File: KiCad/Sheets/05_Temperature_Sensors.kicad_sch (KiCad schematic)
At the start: 7 parts, among them U4 GAS_FLOW_SENSOR, U5 GAS_RETURN_SENSOR, U6 WOOD_FLOW_SENSOR, U7 WOOD_RETURN_SENSOR, U8 WOOD_BOILER_SENSOR

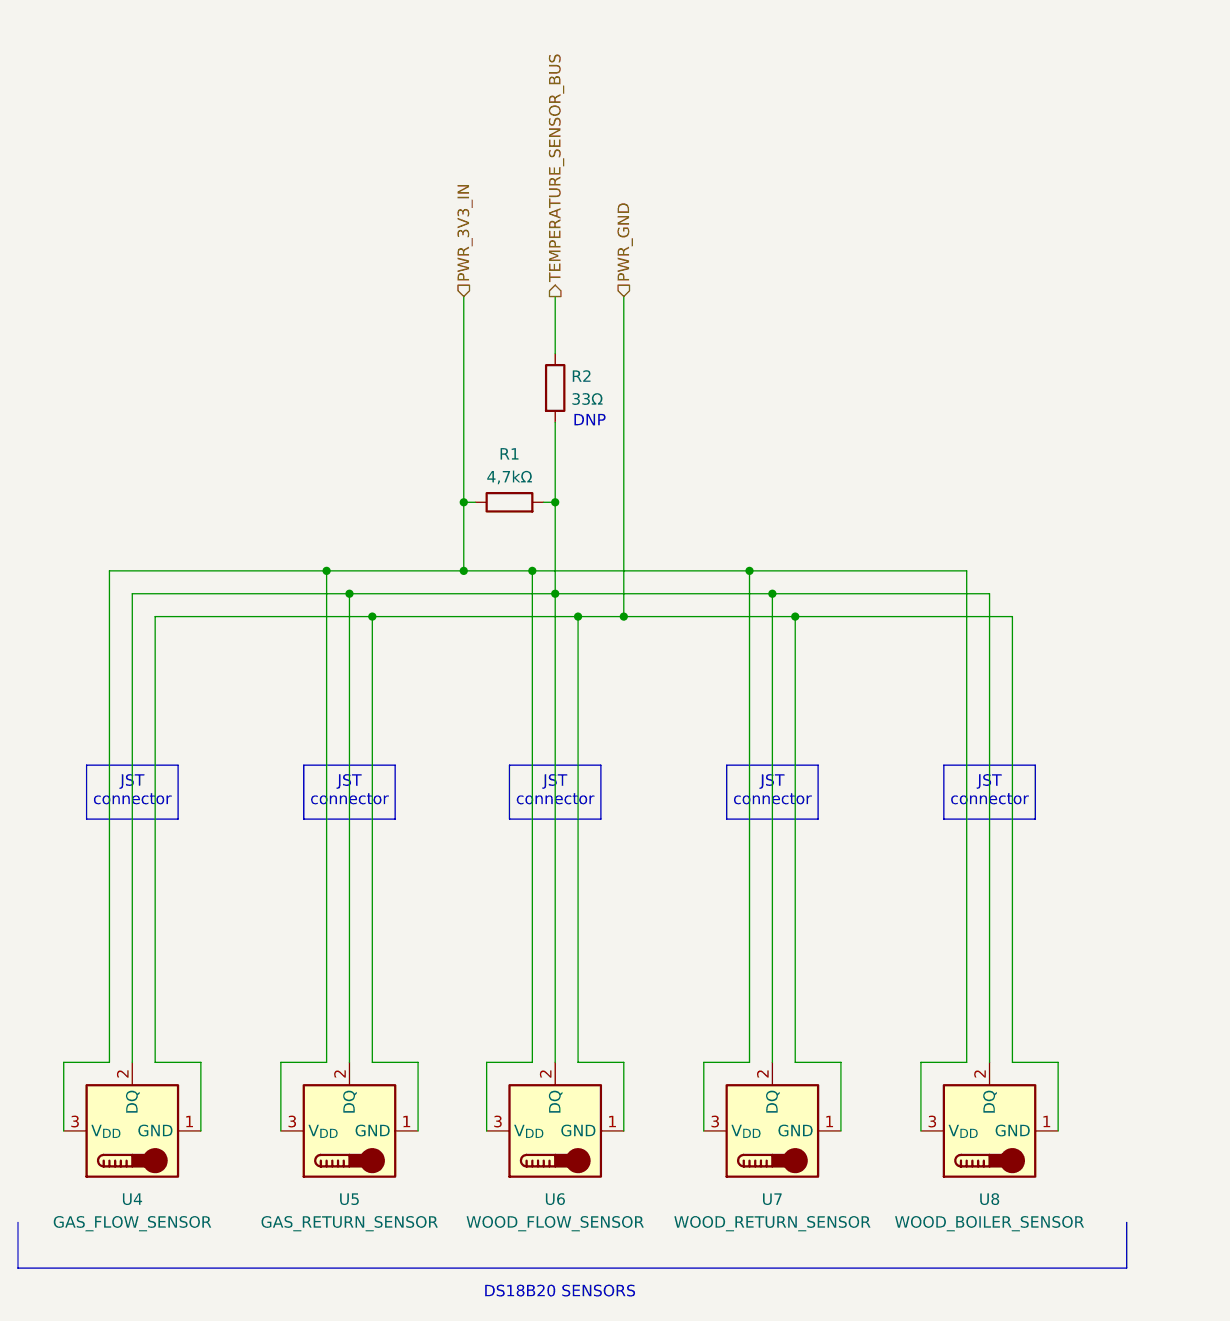
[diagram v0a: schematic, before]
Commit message: Footprints are created and assigned
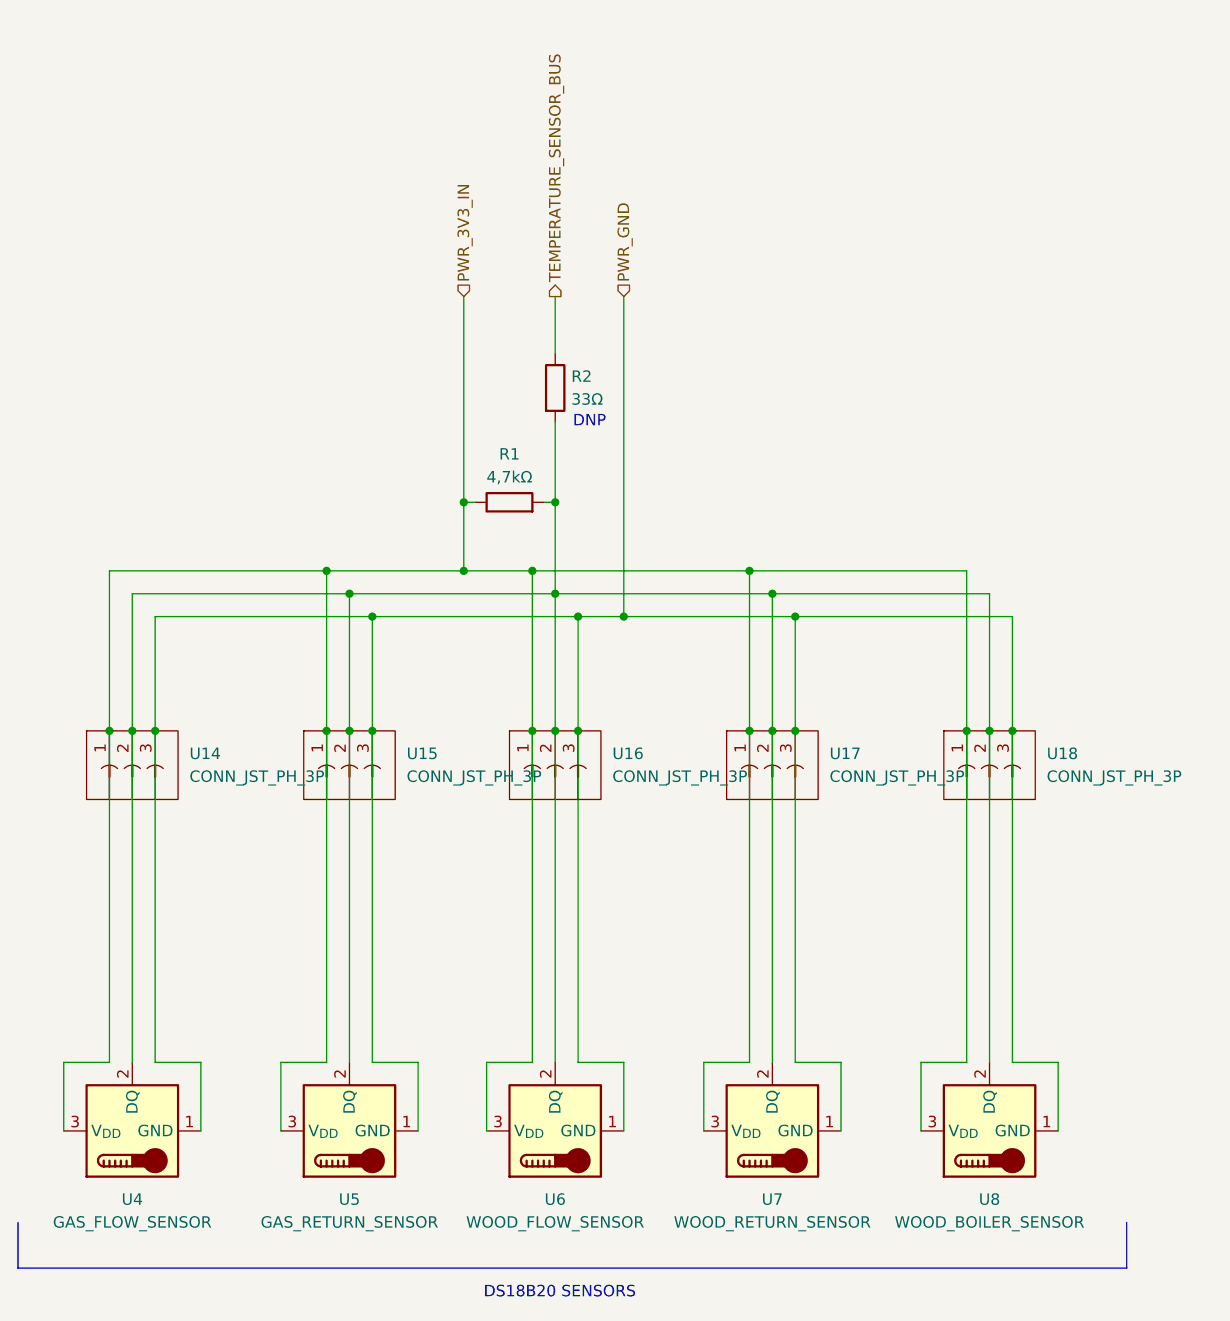
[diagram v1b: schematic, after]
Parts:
- added U14, U15, U16, U17, U18: CONN_JST_PH_3P, Connector_JST:JST_PH_B3B-PH-K_1x03_P2.00mm_Vertical, symbol HMS_Symbols:CONN_JST_PH_3P
- R1, R2: footprint (none) -> Resistor_THT:R_Axial_DIN0207_L6.3mm_D2.5mm_P7.62mm_Horizontal
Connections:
- net PWR_3V3_IN: now also U14.1, U15.1, U16.1, U17.1, U18.1
- net PWR_GND: now also U14.3, U15.3, U16.3, U17.3, U18.3
- net at R1.2, R2.2, U4.2 (DQ)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: now also U14.2, U15.2, U16.2, U17.2, U18.2

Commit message: LEDs sheet added, schematic finished
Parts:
- U14: value CONN_JST_PH_3P -> GAS_FLOW_SENSOR_SOCKET
- U15: value CONN_JST_PH_3P -> GAS_RETURN_SENSOR_SOCKET
- U16: value CONN_JST_PH_3P -> WOOD_FLOW_SENSOR_SOCKET
- U17: value CONN_JST_PH_3P -> WOOD_RETURN_SENSOR_SOCKET
- U18: value CONN_JST_PH_3P -> WOOD_BOILER_SENSOR_SOCKET
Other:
- note removed: "DNP"
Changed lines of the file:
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@@
 	(generator_version "10.0")
 	(paper "A4")
-	(text "DNP"
-		(exclude_from_sim no)
-		(at 151.13 62.23 0)
-		(effects
-			(font
-				(size 1.27 1.27)
-			)
-		)
-	)
 	(text "DS18B20 SENSORS"
 		(exclude_from_sim no)
@@
 		(at 124.46 96.52)
 		(diameter 0)
-		(color 0 0 0 0)
+		(color 255 153 0 1)
 	)
 	(junction
 		(at 171.45 96.52)
 		(diameter 0)
-		(color 0 0 0 0)
+		(color 255 153 0 1)
 	)
 	(junction
@@
 		(at 173.99 96.52)
 		(diameter 0)
-		(color 0 0 0 0)
+		(color 0 0 0 1)
 	)
 	(junction
@@
 		(at 144.78 96.52)
 		(diameter 0)
-		(color 0 0 0 0)
+		(color 255 0 0 1)
 	)
 	(junction
 		(at 147.32 96.52)
 		(diameter 0)
-		(color 0 0 0 0)
+		(color 255 153 0 1)
 	)
 	(junction
 		(at 198.12 96.52)
 		(diameter 0)
-		(color 0 0 0 0)
+		(color 0 0 0 1)
 	)
 	(junction
@@
 		(at 193.04 96.52)
 		(diameter 0)
-		(color 0 0 0 0)
+		(color 255 0 0 1)
 	)
 	(junction
@@
 		(at 168.91 96.52)
 		(diameter 0)
-		(color 0 0 0 0)
+		(color 255 0 0 1)
 	)
 	(junction
 		(at 149.86 96.52)
 		(diameter 0)
-		(color 0 0 0 0)
+		(color 0 0 0 1)
 	)
 	(junction
 		(at 195.58 96.52)
 		(diameter 0)
-		(color 0 0 0 0)
+		(color 255 153 0 1)
 	)
 	(junction
 		(at 97.79 96.52)
 		(diameter 0)
-		(color 0 0 0 0)
+		(color 255 0 0 1)
 	)
 	(junction
 		(at 100.33 96.52)
 		(diameter 0)
-		(color 0 0 0 0)
+		(color 255 153 0 1)
 	)
 	(junction
@@
 		(at 127 96.52)
 		(diameter 0)
-		(color 0 0 0 0)
+		(color 0 0 0 1)
 	)
 	(junction
@@
 		(at 121.92 96.52)
 		(diameter 0)
-		(color 0 0 0 0)
+		(color 255 0 0 1)
 	)
 	(junction
 		(at 102.87 96.52)
 		(diameter 0)
-		(color 0 0 0 0)
+		(color 0 0 0 1)
 	)
 	(junction
@@
 		(in_pos_files yes)
 		(dnp no)
-		(fields_autoplaced yes)
 		(property "Reference" "U15"
 			(at 130.81 99.0599 0)
@@
 			)
 		)
-		(property "Value" "CONN_JST_PH_3P"
-			(at 130.81 101.5999 0)
+		(property "Value" "GAS_RETURN_SENSOR_SOCKET"
+			(at 110.744 93.726 0)
 			(show_name no)
 			(do_not_autoplace no)
@@
 		(in_pos_files yes)
 		(dnp no)
-		(fields_autoplaced yes)
 		(property "Reference" "U14"
 			(at 106.68 99.0599 0)
@@
 			)
 		)
-		(property "Value" "CONN_JST_PH_3P"
-			(at 106.68 101.5999 0)
+		(property "Value" "GAS_FLOW_SENSOR_SOCKET"
+			(at 89.154 105.918 0)
 			(show_name no)
 			(do_not_autoplace no)
@@
 		(in_pos_files yes)
 		(dnp no)
-		(fields_autoplaced yes)
 		(property "Reference" "U16"
 			(at 153.67 99.0599 0)
@@
 			)
 		)
-		(property "Value" "CONN_JST_PH_3P"
-			(at 153.67 101.5999 0)
+		(property "Value" "WOOD_FLOW_SENSOR_SOCKET"
+			(at 134.112 106.172 0)
 			(show_name no)
 			(do_not_autoplace no)
@@
 		(in_pos_files yes)
 		(dnp no)
-		(fields_autoplaced yes)
 		(property "Reference" "U18"
 			(at 201.93 99.0599 0)
@@
 			)
 		)
-		(property "Value" "CONN_JST_PH_3P"
-			(at 201.93 101.5999 0)
+		(property "Value" "WOOD_BOILER_SENSOR_SOCKET"
+			(at 180.848 105.918 0)
 			(show_name no)
 			(do_not_autoplace no)
@@
 		(in_pos_files yes)
 		(dnp no)
-		(fields_autoplaced yes)
 		(property "Reference" "U17"
 			(at 177.8 99.0599 0)
@@
 			)
 		)
-		(property "Value" "CONN_JST_PH_3P"
-			(at 177.8 101.5999 0)
-			(show_name no)
-			(do_not_autoplace no)
+		(property "Value" "WOOD_RETURN_SENSOR_SOCKET"
+			(at 155.956 94.234 0)
+			(show_name no)
+			(do_not_autoplace no)

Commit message: Finished PCB
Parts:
- removed U15: GAS_RETURN_SENSOR_SOCKET, Connector_JST:JST_PH_B3B-PH-K_1x03_P2.00mm_Vertical, symbol HMS_Symbols:CONN_JST_PH_3P
- removed U16: WOOD_FLOW_SENSOR_SOCKET, Connector_JST:JST_PH_B3B-PH-K_1x03_P2.00mm_Vertical, symbol HMS_Symbols:CONN_JST_PH_3P
- removed U17: WOOD_RETURN_SENSOR_SOCKET, Connector_JST:JST_PH_B3B-PH-K_1x03_P2.00mm_Vertical, symbol HMS_Symbols:CONN_JST_PH_3P
- U14: value GAS_FLOW_SENSOR_SOCKET -> PIPE_SENSORS_SOCKET; footprint Connector_JST:JST_PH_B3B-PH-K_1x03_P2.00mm_Vertical -> Connector_JST:JST_XH_B3B-XH-A_1x03_P2.50mm_Vertical
- U18: footprint Connector_JST:JST_PH_B3B-PH-K_1x03_P2.00mm_Vertical -> Connector_JST:JST_XH_B3B-XH-A_1x03_P2.50mm_Vertical
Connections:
- net at R1.2, R2.2, U14.2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: no longer U4.2 (DQ), U5.2 (DQ), U7.2 (DQ)
- new net: U4.2 (DQ), U5.2 (DQ), U7.2 (DQ)
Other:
- moved on the sheet: U14, U18
